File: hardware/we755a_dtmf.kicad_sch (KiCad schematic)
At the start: 44 parts, among them J1 Conn_01x06_Male, J2 UPDI, J3 Conn_02x10_Odd_Even, U1 AVR128DA28-I/SS, U2 MT8870, U3 H11AA1, U4 LAA108, U5 LAA108, U6 LAA108, U7 LAA108, U8 LAA108, Y1 32.767KHz, Y2 3.579545MHZ

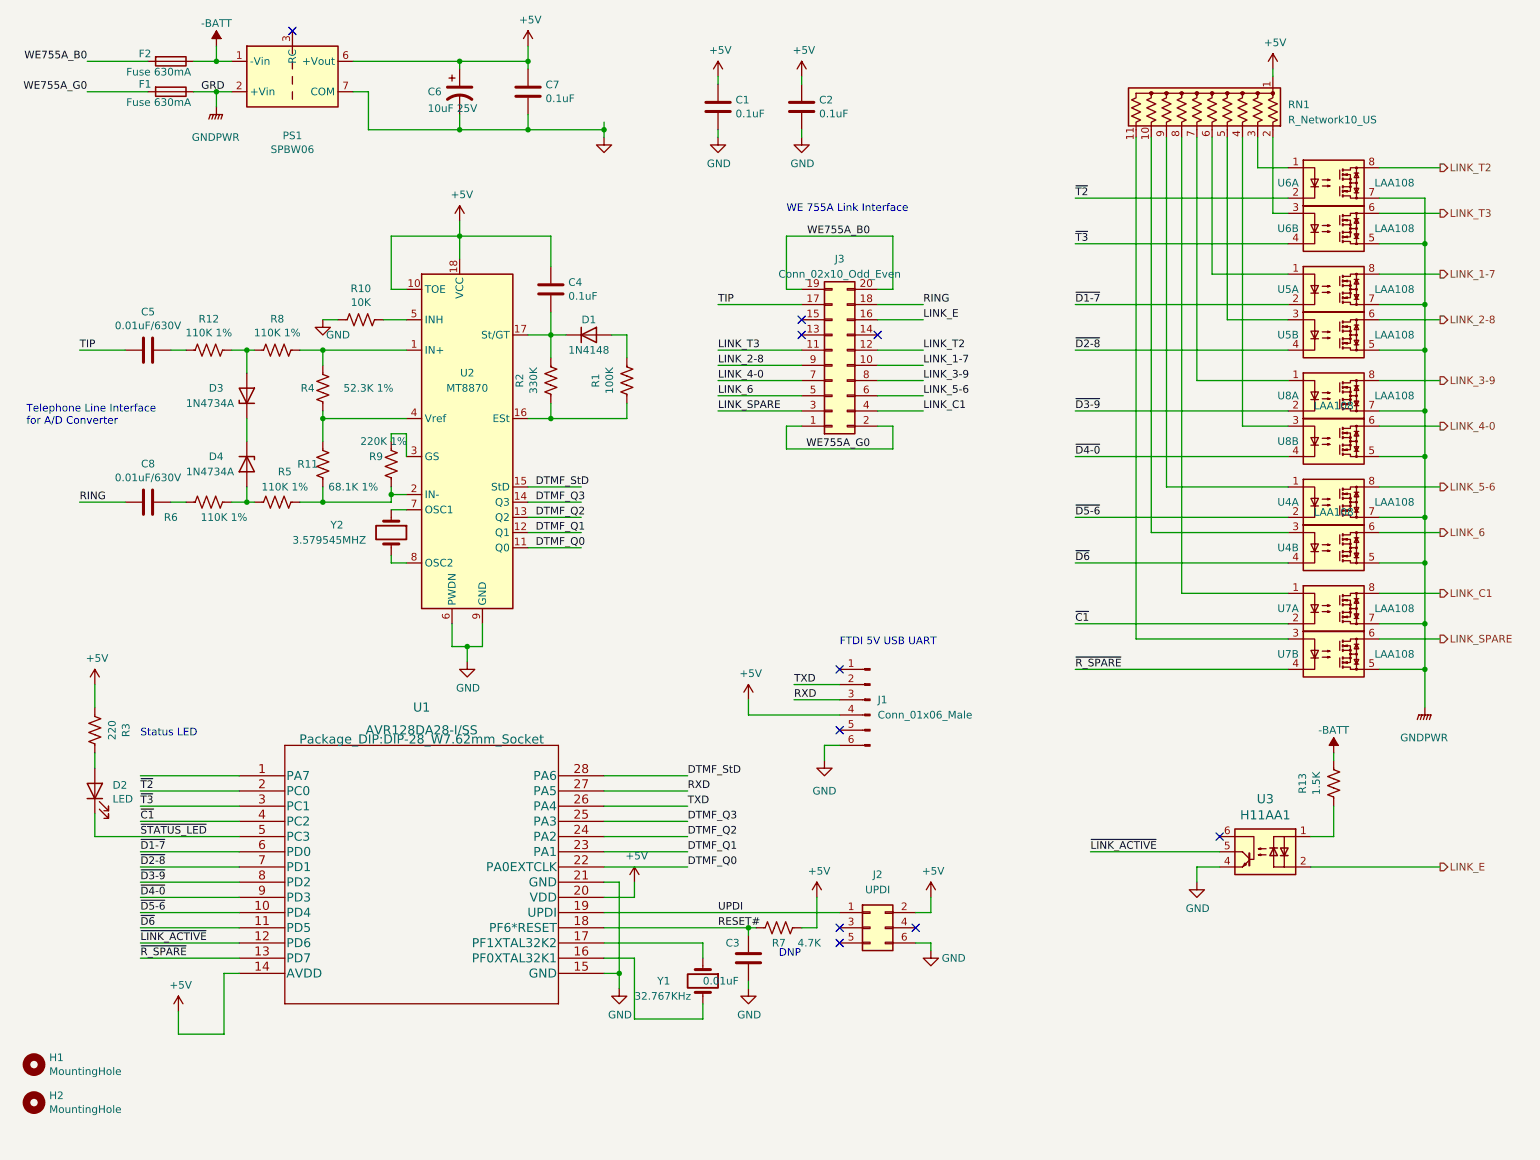
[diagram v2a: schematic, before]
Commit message: Issue 3: Smaller board.     * Smaller board.     * Jumper options for DTMF converter and station concentrator.
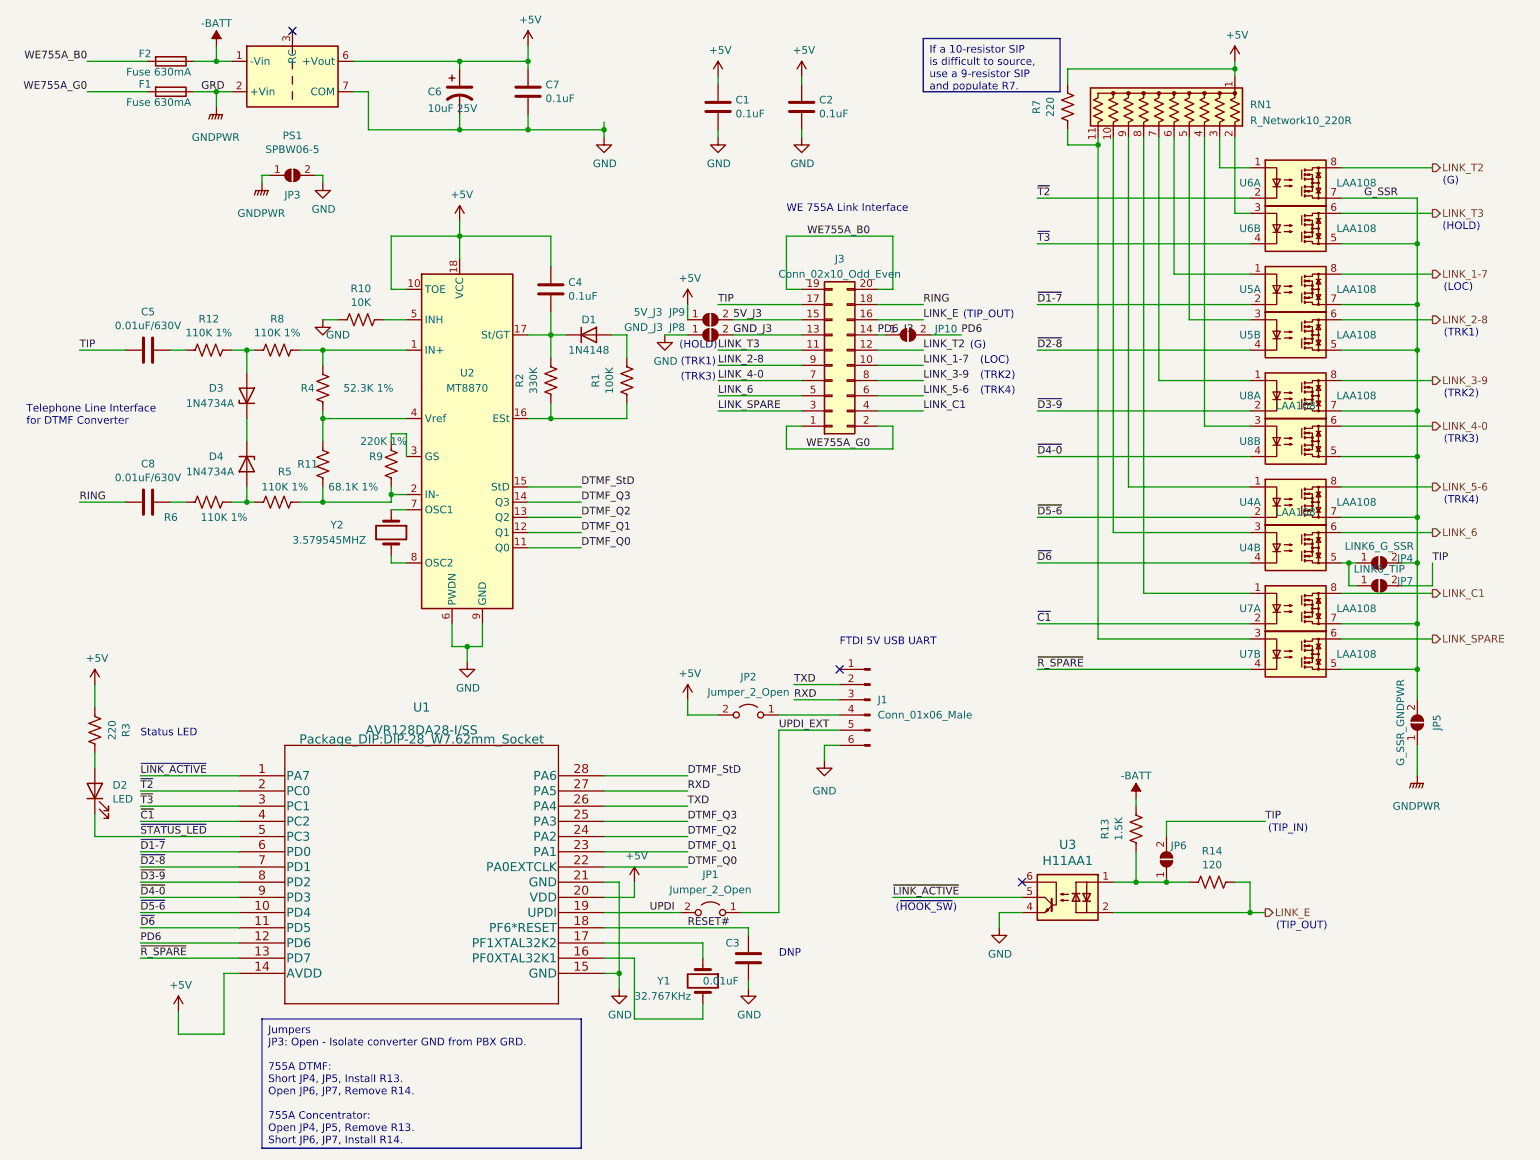
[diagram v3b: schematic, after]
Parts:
- removed H1, H2: MountingHole, MountingHole:MountingHole_2.7mm_Pad, symbol Mechanical:MountingHole
- removed J2: UPDI, Connector_PinHeader_2.54mm:PinHeader_2x03_P2.54mm_Vertical, symbol Connector_Generic:Conn_02x03_Odd_Even
- added JP1, JP2: Jumper_2_Open, Connector_PinHeader_2.54mm:PinHeader_1x02_P2.54mm_Vertical, symbol Jumper:Jumper_2_Open
- added JP10, JP9: 5V_J3, Jumper:SolderJumper-2_P1.3mm_Open_Pad1.0x1.5mm, symbol Jumper:SolderJumper_2_Open
- added JP3: GRD_TIE, Jumper:SolderJumper-2_P1.3mm_Open_Pad1.0x1.5mm, symbol Jumper:SolderJumper_2_Open
- added JP4: LINK6_G_SSR, Jumper:SolderJumper-2_P1.3mm_Open_Pad1.0x1.5mm, symbol Jumper:SolderJumper_2_Open
- added JP5: G_SSR_GNDPWR, Jumper:SolderJumper-2_P1.3mm_Open_Pad1.0x1.5mm, symbol Jumper:SolderJumper_2_Open
- added JP6: TIP_IN, Jumper:SolderJumper-2_P1.3mm_Open_Pad1.0x1.5mm, symbol Jumper:SolderJumper_2_Open
- added JP7: LINK6_TIP, Jumper:SolderJumper-2_P1.3mm_Open_Pad1.0x1.5mm, symbol Jumper:SolderJumper_2_Open
- added JP8: GND_J3, Jumper:SolderJumper-2_P1.3mm_Open_Pad1.0x1.5mm, symbol Jumper:SolderJumper_2_Open
- added R14: 120, Resistor_THT:R_Axial_DIN0207_L6.3mm_D2.5mm_P7.62mm_Horizontal, symbol Device:R_US
- C3: Digi-Key_PN (none) -> BC5227CT-ND; MPN (none) -> K103K15X7RF5UL2
- C6: Digi-Key_PN (none) -> P19534CT-ND; MPN (none) -> ECA-1JM100I
- C7: Digi-Key_PN (none) -> 56-K104M15X7RF5TL2CT-ND; Digi-Key_PN  56-K104M15X7RF5TL2CT-ND -> (none)
- D1: Digi-Key_PN (none) -> 1N4148TACT-ND; MPN (none) -> 1N4148TA
- D2: Digi-Key_PN (none) -> 1497-1031-ND; MPN (none) -> XLUR12D
- F1, F2: footprint Resistor_THT:R_Axial_DIN0309_L9.0mm_D3.2mm_P12.70mm_Horizontal -> Resistor_THT:R_Axial_DIN0207_L6.3mm_D2.5mm_P10.16mm_Horizontal; Digi-Key_PN (none) -> F2312-ND; MPN (none) -> 0251.630MXL
- J1: Digi-Key_PN (none) -> 732-5339-ND; MPN (none) -> 61300611021
- J3: footprint Connector_PinHeader_2.54mm:PinHeader_2x10_P2.54mm_Vertical -> ac125a_dtmf:WE755A-DTMF; Digi-Key_PN (none) -> S9180-ND; MPN (none) -> SBH11-PBPC-D10-RA-BK
- PS1: value SPBW06 -> SPBW06-5; Digi-Key_PN (none) -> 1866-4814-ND; MPN (none) -> SPBW06G-05
- R1: Digi-Key_PN (none) -> S100KHCT-ND; MPN (none) -> CFM12JT100K
- R10: Digi-Key_PN (none) -> S10KHCT-ND; MPN (none) -> CFM12JT10K0
- R11: Digi-Key_PN (none) -> 68.1KXBK-ND; MPN (none) -> MFR-25FBF52-68K1
- R13: Digi-Key_PN (none) -> S1.5KHCT-ND; MPN (none) -> CFM12JT1K50
- R2: Digi-Key_PN (none) -> S330KHCT-ND; MPN (none) -> CFM12JT330K
- R3: Digi-Key_PN (none) -> S220QCT-ND; MPN (none) -> CFM14JT220R
- R4: Digi-Key_PN (none) -> 52.3KXBK-ND; MPN (none) -> MFR-25FBF52-52K3
- R7: value 4.7K -> 220; footprint Resistor_THT:R_Axial_DIN0207_L6.3mm_D2.5mm_P7.62mm_Horizontal -> Resistor_THT:R_Axial_DIN0204_L3.6mm_D1.6mm_P5.08mm_Horizontal; Digi-Key_PN (none) -> S220QCT-ND; MPN (none) -> CFM14JT220R
- R9: Digi-Key_PN (none) -> MFR-25FBF52-220K-ND; MPN (none) -> MFR-25FBF52-220K
- RN1: value R_Network10_US -> R_Network10_220R; Digi-Key_PN (none) -> 118-4611X-101-221LF-ND; MPN (none) -> 4611X-101-221LF
- U1: Digi-Key_PN (none) -> 150-AVR128DA28-E/SP-ND; MPN (none) -> AVR128DA28-E/SP
- U4, U5, U6, U7, U8: Digi-Key_PN (none) -> LAA108-ND; MPN (none) -> LAA108
- Y1: Digi-Key_PN (none) -> Do not populate.; MPN (none) -> Do not populate.
- Y2: Digi-Key_PN (none) -> 887-1000-ND; MPN (none) -> 9B-3.579545MAAJ-B
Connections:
- net +5V: now also JP2.2 (B), JP9.1 (A); no longer J1.4 (Pin_4)
- net GND: now also JP3.2 (B), JP8.1 (A)
- net GNDPWR: now also JP3.1 (A), JP5.1 (A); no longer U4.5, U4.7, U5.5, U5.7, U6.5, U6.7, U7.5, U7.7, U8.5, U8.7
- net LINK_E: now also R14.1
- net RESET#: no longer R7.2
- net TIP: now also JP6.2 (B), JP7.2 (B)
- net UPDI: now also JP1.2 (B)
- net ~{LINK_ACTIVE}: now also U1.1 (PA7); no longer U1.12 (PD6)
- net at R13.2, U3.1: now also JP6.1 (A), R14.2
- net UPDI_EXT: now reaches J1.5 (Pin_5)
- net UPDI_EXT: now also JP1.1 (A)
- net at RN1.11 (R10), U7.3: now also R7.2
- net GND_J3: now reaches J3.13 (Pin_13)
- net GND_J3: now also JP8.2 (B)
- net PD6_J3: now reaches J3.14 (Pin_14)
- net PD6_J3: now also JP10.1 (A)
- net 5V_J3: now reaches J3.15 (Pin_15)
- net 5V_J3: now also JP9.2 (B)
- new net: JP4.1 (A), JP7.1 (A), U4.5
- new net: J1.4 (Pin_4), JP2.1 (A)
- new net G_SSR: JP4.2 (B), JP5.2 (B), U4.7, U5.5, U5.7, U6.5, U6.7, U7.5, U7.7, U8.5, U8.7
- new net PD6: JP10.2 (B), U1.12 (PD6)
- no-connect marks 10 -> 3
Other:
- note added: "(G)"
- note added: "(HOLD)"
- note added: "(LOC)"
- note added: "(TIP_IN)"
- note added: "(TIP_OUT)"
- note added: "(TRK1)"
- note added: "(TRK2)"
- note added: "(TRK3)"
- note added: "(TRK4)"
- note added: "(~{HOOK_SW})"
- note added: "Telephone Line Interface for DTMF Converter"
- note removed: "Telephone Line Interface for A/D Converter"
- moved on the sheet: R13, RN1, U3, U4A, U4B, U5A, U5B, U6A, U6B, U7A, U7B, U8A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

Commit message: Issue 4: Change fuses to PTCs.
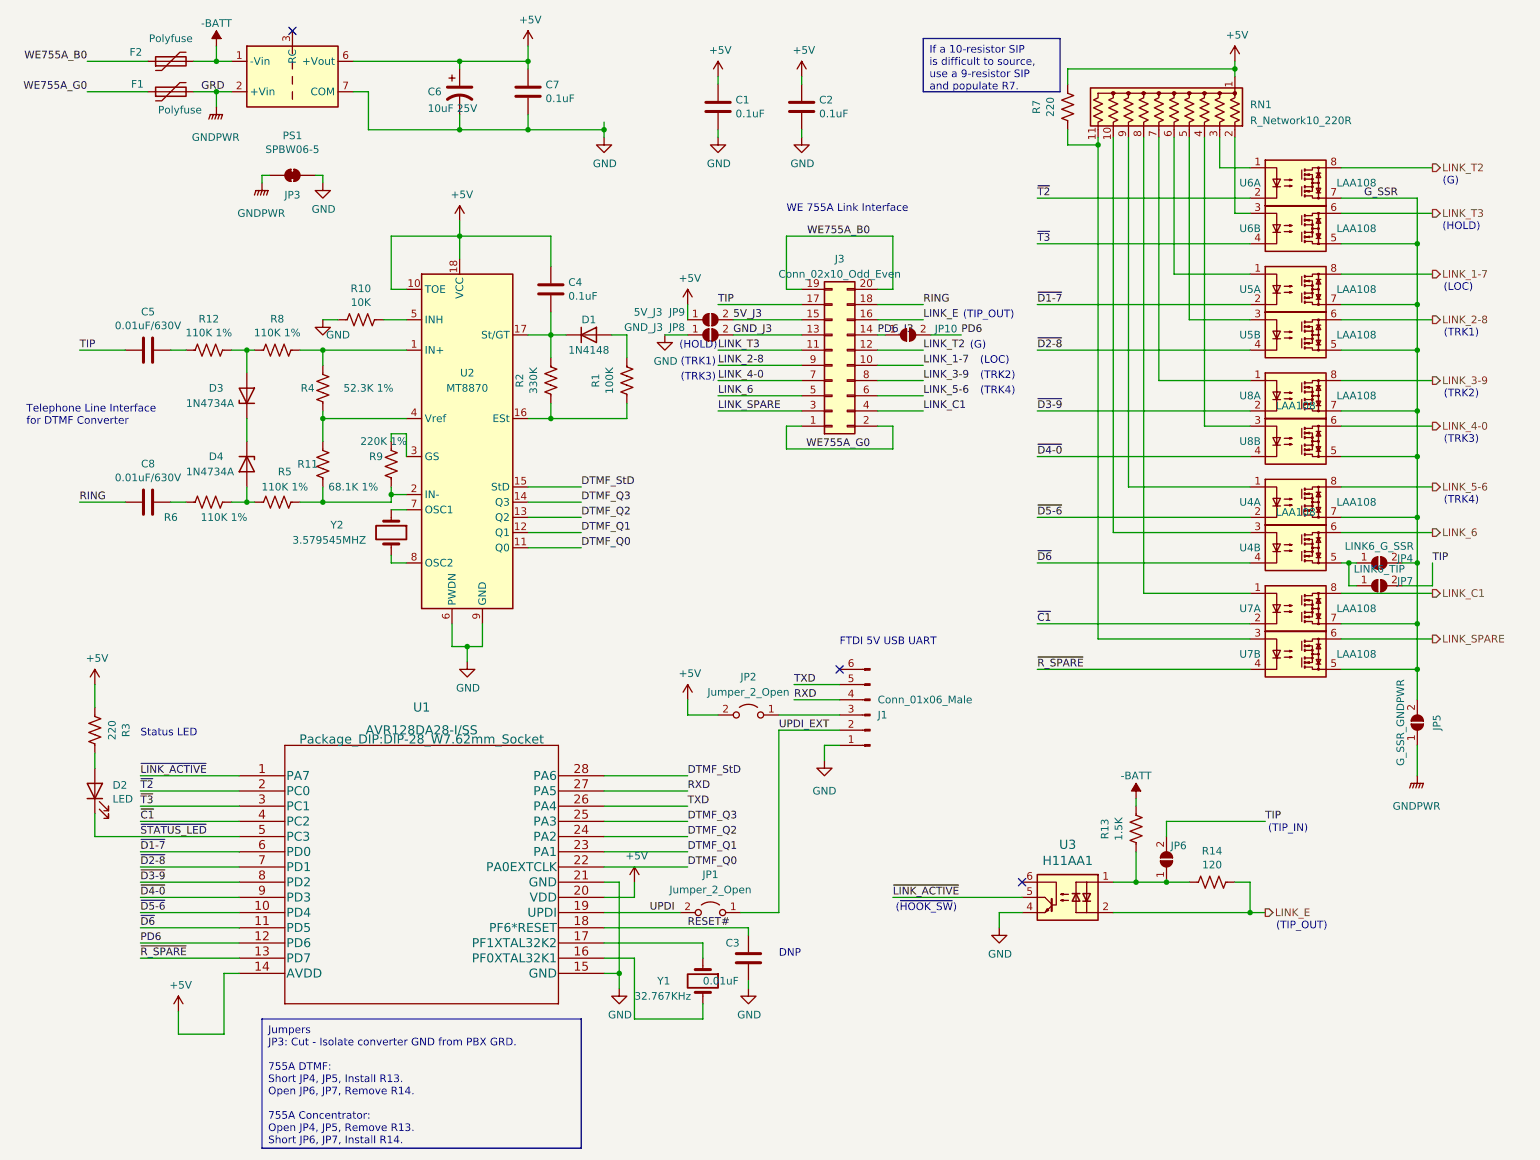
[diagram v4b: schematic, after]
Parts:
- removed F1, F2: Fuse 630mA, Resistor_THT:R_Axial_DIN0207_L6.3mm_D2.5mm_P10.16mm_Horizontal, symbol Device:Fuse
- added F1, F2: Polyfuse, ac125a_dtmf:FUSE_RXEF025_LTF, symbol Device:Polyfuse
- JP3: footprint Jumper:SolderJumper-2_P1.3mm_Open_Pad1.0x1.5mm -> Jumper:SolderJumper-2_P1.3mm_Bridged_Pad1.0x1.5mm; symbol Jumper:SolderJumper_2_Open -> Jumper:SolderJumper_2_Bridged
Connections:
- net -BATT: now also F2.2
- net GND: now also J1.1 (Pin_1); no longer J1.6 (Pin_6)
- net GNDPWR: now also F1.2
- net RXD: now also J1.4 (Pin_4); no longer J1.3 (Pin_3)
- net TXD: now also J1.5 (Pin_5); no longer J1.2 (Pin_2)
- net UPDI_EXT: now also J1.2 (Pin_2); no longer J1.5 (Pin_5)
- net WE755A_B0: now also F2.1
- net WE755A_G0: now also F1.1
- net at JP2.1 (A): now also J1.3 (Pin_3); no longer J1.4 (Pin_4)
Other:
- moved on the sheet: JP3

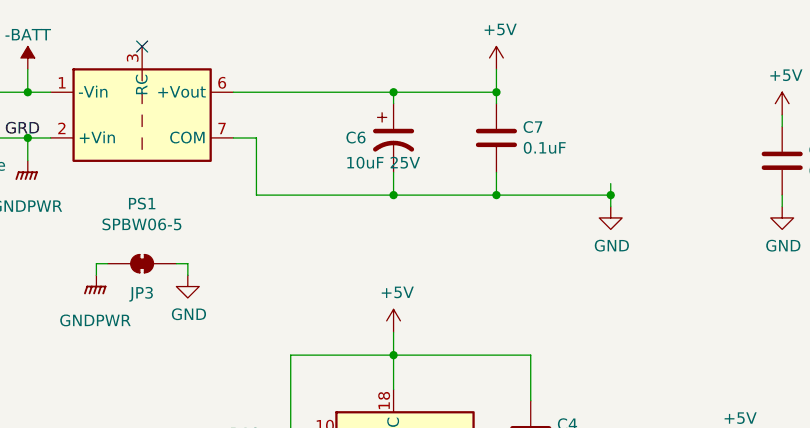
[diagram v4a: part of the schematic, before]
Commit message: Change C6 from electrolytic to ceramic.
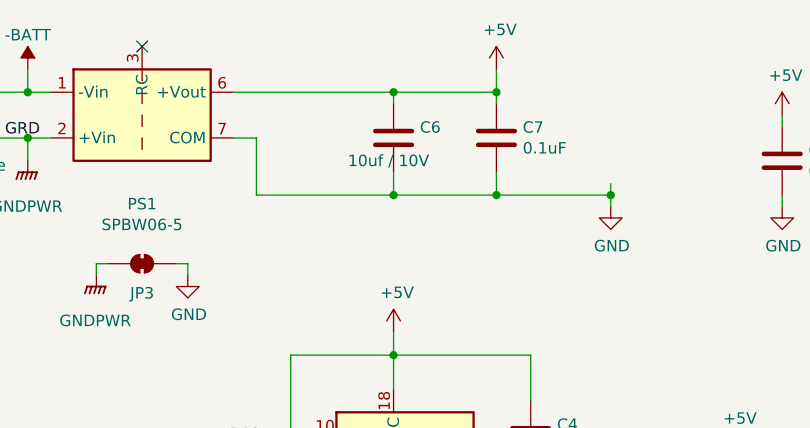
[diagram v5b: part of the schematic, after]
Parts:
- removed C6: 10uF 25V, Capacitor_THT:CP_Radial_D6.3mm_P2.50mm, symbol ac125a_dtmf-rescue:CP1-Device
- added C6: 10uf / 10V, Capacitor_THT:C_Disc_D5.0mm_W2.5mm_P2.50mm, symbol Device:C
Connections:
- net +5V: now also C6.1
- net GND: now also C6.2
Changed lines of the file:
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@@
-	)
-	(symbol
-		(lib_id "ac125a_dtmf-rescue:CP1-Device")
-		(at 90.17 25.4 0)
-		(unit 1)
-		(exclude_from_sim no)
-		(in_bom yes)
-		(on_board yes)
-		(dnp no)
-		(property "Reference" "C6"
-			(at 84.836 25.4 0)
-			(effects
-				(font
-					(size 1.27 1.27)
-				)
-				(justify left)
-			)
-		)
-		(property "Value" "10uF 25V"
-			(at 84.836 28.194 0)
-			(effects
-				(font
-					(size 1.27 1.27)
-				)
-				(justify left)
-			)
-		)
-		(property "Footprint" "Capacitor_THT:CP_Radial_D6.3mm_P2.50mm"
-			(at 90.17 25.4 0)
-			(effects
-				(font
-					(size 1.27 1.27)
-				)
-				(hide yes)
-			)
-		)
-		(property "Datasheet" "~"
-			(at 90.17 25.4 0)
-			(effects
-				(font
-					(size 1.27 1.27)
-				)
-				(hide yes)
-			)
-		)
-		(property "Description" ""
-			(at 90.17 25.4 0)
-			(effects
-				(font
-					(size 1.27 1.27)
-				)
-				(hide yes)
-			)
-		)
-		(property "Digi-Key_PN" "P19534CT-ND"
-			(at 90.17 25.4 0)
-			(effects
-				(font
-					(size 1.27 1.27)
-				)
-				(hide yes)
-			)
-		)
-		(property "MPN" "ECA-1JM100I"
-			(at 90.17 25.4 0)
-			(effects
-				(font
-					(size 1.27 1.27)
-				)
-				(hide yes)
-			)
-		)
-		(pin "1"
-		)
-		(pin "2"
-		)
-		(instances
-			(project "we755a_dtmf"
-				(path "/1da82a49-7ca3-4401-a29b-3550e75481e8"
-					(reference "C6")
-					(unit 1)
-				)
-			)
-		)
 	)
 	(symbol
@@
 					(unit 1)
 				)
+			)
+		)
+	)
+	(symbol
+		(lib_id "Device:C")
+		(at 90.17 25.4 0)
+		(unit 1)
+		(exclude_from_sim no)
+		(in_bom yes)
+		(on_board yes)
+		(dnp no)
+		(property "Reference" "C6"
+			(at 93.091 24.2316 0)
+			(effects
+				(font
+					(size 1.27 1.27)
+				)
+				(justify left)
+			)
+		)
+		(property "Value" "10uf / 10V"
+			(at 85.09 27.94 0)
+			(effects
+				(font
+					(size 1.27 1.27)
+				)
+				(justify left)
+			)
+		)
+		(property "Footprint" "Capacitor_THT:C_Disc_D5.0mm_W2.5mm_P2.50mm"
+			(at 91.1352 29.21 0)
+			(effects
+				(font
+					(size 1.27 1.27)
+				)
+				(hide yes)
+			)
+		)
+		(property "Datasheet" "~"
+			(at 90.17 25.4 0)
+			(effects
+				(font
+					(size 1.27 1.27)
+				)
+				(hide yes)
+			)
+		)
+		(property "Description" ""
+			(at 90.17 25.4 0)
+			(effects
+				(font
+					(size 1.27 1.27)
+				)
+				(hide yes)
+			)
+		)
+		(property "MPN" "FG14X7R1A106KRT06"
+			(at 90.17 25.4 0)
+			(effects
+				(font
+					(size 1.27 1.27)
+				)
+				(hide yes)
+			)
+		)
+		(property "Digi-Key_PN" "445-173132-1-ND"
+			(at 90.17 25.4 0)
+			(effects
+				(font
+					(size 1.27 1.27)
+				)
+				(hide yes)
+			)
+		)
+		(pin "1"
+		)
+		(pin "2"
+		)
+		(instances
+			(project "we755a_dtmf"
+				(path "/1da82a49-7ca3-4401-a29b-3550e75481e8"
+					(reference "C6")
+					(unit 1)
+				)
